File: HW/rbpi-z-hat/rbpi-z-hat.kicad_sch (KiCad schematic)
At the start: 0 parts

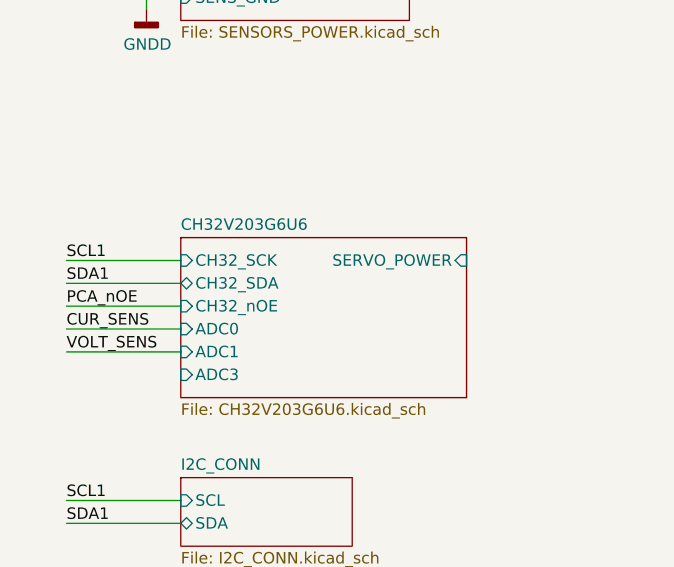
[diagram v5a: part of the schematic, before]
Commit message: Updated CH32V203G6U6.kicad_sch
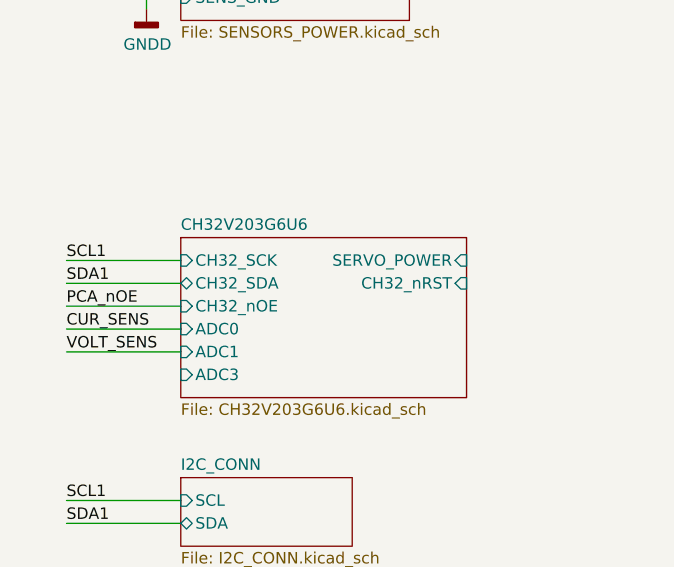
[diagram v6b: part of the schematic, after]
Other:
- sheet CH32V203G6U6 ports: added CH32_nRST; removed none
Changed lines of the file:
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@@
       (effects (font (size 1.27 1.27)) (justify left))
+    )
+    (pin "CH32_nRST" input (at 163.83 134.62 0)
+      (effects (font (size 1.27 1.27)) (justify right))
     )
     (instances

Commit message: Update
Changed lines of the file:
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@@
+    (stroke (width 0) (type default))
+  )
+  (wire (pts (xy 74.93 102.87) (xy 87.63 102.87))
     (stroke (width 0) (type default))
   )
@@
     (effects (font (size 1.27 1.27)) (justify left bottom))
   )
+  (label "MS_nCS" (at 87.63 102.87 180) (fields_autoplaced)
+    (effects (font (size 1.27 1.27)) (justify right bottom))
+  )
   (label "SENS_FGND" (at 149.86 40.64 0) (fields_autoplaced)
     (effects (font (size 1.27 1.27)) (justify left bottom))
@@
     (effects (font (size 1.27 1.27)) (justify right bottom))
   )
+  (label "MS_nCS" (at 119.38 78.74 0) (fields_autoplaced)
+    (effects (font (size 1.27 1.27)) (justify left bottom))
+  )
   (label "SENS_SCK" (at 91.44 161.29 180) (fields_autoplaced)
